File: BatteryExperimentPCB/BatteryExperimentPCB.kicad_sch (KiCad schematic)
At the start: 32 parts, among them J1 USB_C_Receptacle_USB2.0_14P, J2 Conn_01x12_Pin, J3 Conn_01x12_Pin, Q1 DMG1012T, SW1 SW_Push, U1 ATtiny3226-M, U2 USBLC6-2P6, U3 BQ25628RYKR

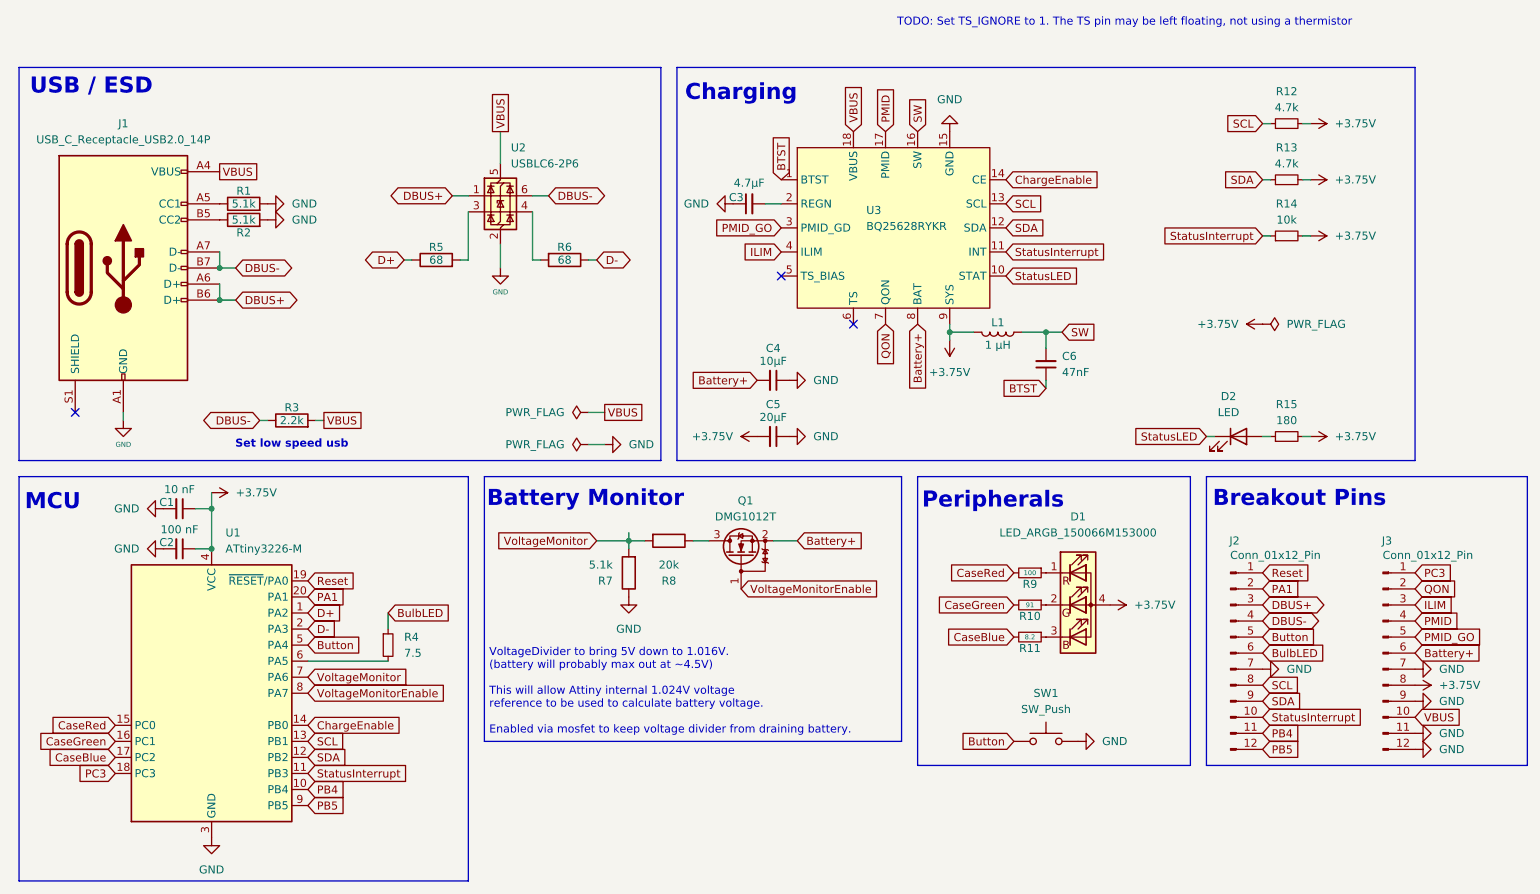
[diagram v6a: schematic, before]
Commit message: updating comment, changing pin breakout order
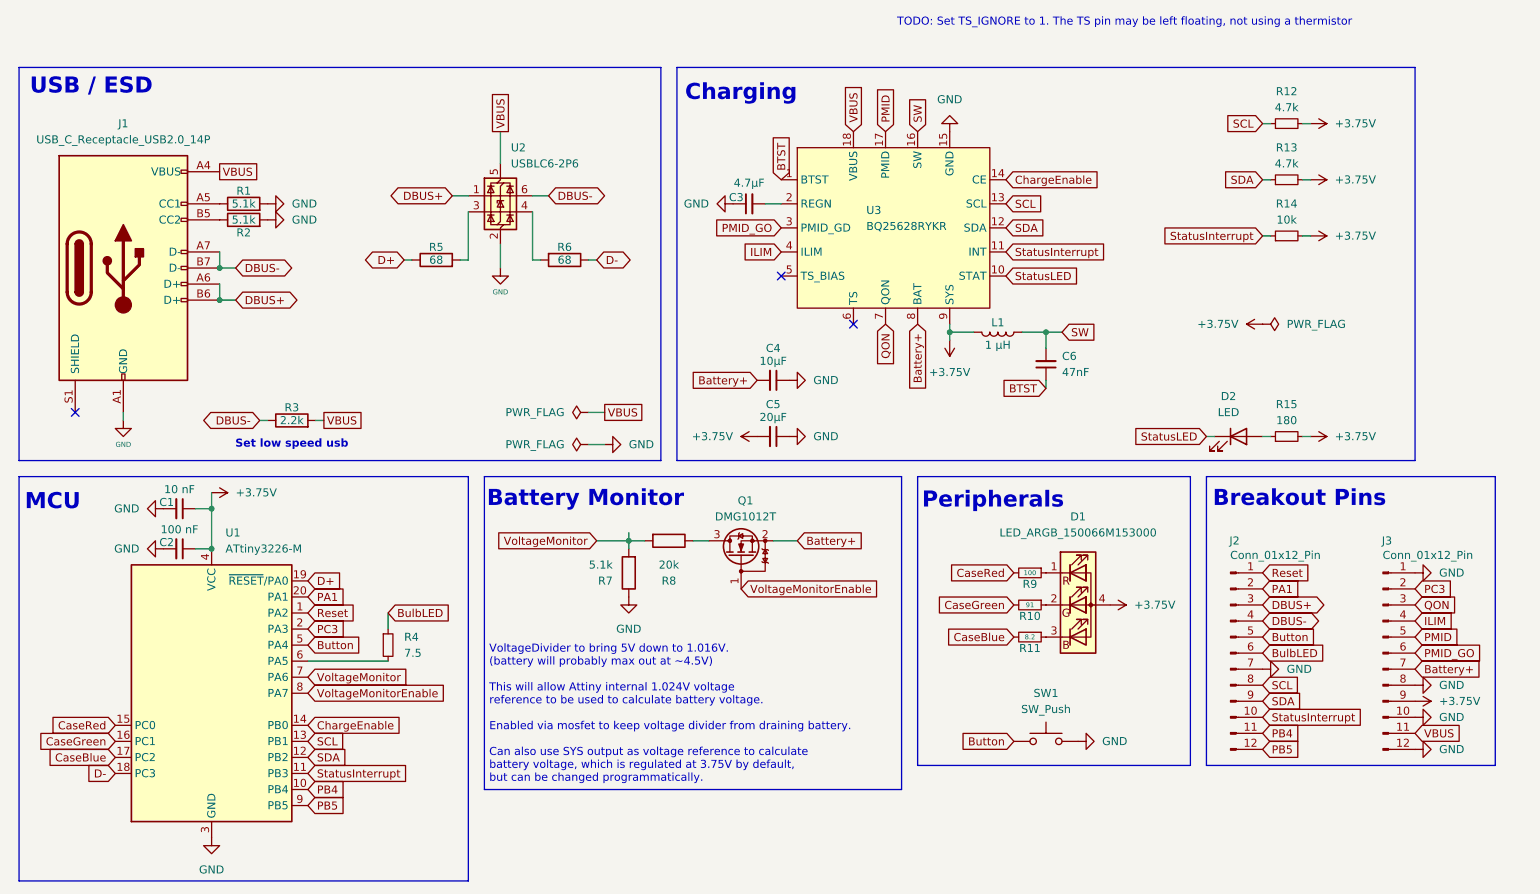
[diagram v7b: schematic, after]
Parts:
- C1, C2, C3, C4, C5, C6: footprint Capacitor_SMD:C_0805_2012Metric -> Capacitor_SMD:C_0603_1608Metric
- R1, R10, R11, R12, R13, R14, R15, R2, R3, R4, R5, R6, R7, R8, R9, SW1: footprint Resistor_SMD:R_0805_2012Metric -> Resistor_SMD:R_0603_1608Metric
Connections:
- net +3.75V: now also J3.9 (Pin_9); no longer J3.8 (Pin_8)
- net Battery+: now also J3.7 (Pin_7); no longer J3.6 (Pin_6)
- net D+: now also U1.19 (~{RESET}/PA0); no longer U1.1 (PA2)
- net D-: now also U1.18 (PC3); no longer U1.2 (PA3)
- net GND: now also J3.1 (Pin_1), J3.10 (Pin_10), J3.8 (Pin_8); no longer J3.11 (Pin_11), J3.7 (Pin_7), J3.9 (Pin_9)
- net ILIM: now also J3.4 (Pin_4); no longer J3.3 (Pin_3)
- net PC3: now also J3.2 (Pin_2), U1.2 (PA3); no longer J3.1 (Pin_1), U1.18 (PC3)
- net PMID: now also J3.5 (Pin_5); no longer J3.4 (Pin_4)
- net PMID_GO: now also J3.6 (Pin_6); no longer J3.5 (Pin_5)
- net QON: now also J3.3 (Pin_3); no longer J3.2 (Pin_2)
- net Reset: now also U1.1 (PA2); no longer U1.19 (~{RESET}/PA0)
- net VBUS: now also J3.11 (Pin_11); no longer J3.10 (Pin_10)
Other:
- note added: "VoltageDivider to bring 5V down to 1.016V. (battery will probably max out at ~4.5V) This will allow Attiny internal 1.024V voltage reference to be used to calculate battery voltage. Enabled via mosfet to keep voltage divider from draining battery. Can also use SYS output as voltage reference to calculate battery voltage, which is regulated at 3.75V by default, but can be changed programmatically."
- note removed: "VoltageDivider to bring 5V down to 1.016V. (battery will probably max out at ~4.5V) This will allow Attiny internal 1.024V voltage reference to be used to calculate battery voltage. Enabled via mosfet to keep voltage divider from draining battery."

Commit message: more pcb work
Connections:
- net Button: now also J2.2 (Pin_2), U1.2 (PA3); no longer J2.5 (Pin_5), U1.5 (PA4)
- net PA1: now also J2.5 (Pin_5); no longer J2.2 (Pin_2)
- net PC3 renamed PA4
- net PA4: now also U1.5 (PA4); no longer U1.2 (PA3)
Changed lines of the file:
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@@
-		)
-	)
-	(global_label "Button"
-		(shape input)
-		(at 59.69 105.41 0)
-		(fields_autoplaced yes)
-		(effects
-			(font
-				(size 1.27 1.27)
-			)
-			(justify left)
-		)
-		(property "Intersheetrefs" "${INTERSHEET_REFS}"
-			(at 68.8436 105.41 0)
-			(effects
-				(font
-					(size 1.27 1.27)
-				)
-				(justify left)
-				(hide yes)
-			)
 		)
 	)
@@
 		)
 	)
-	(global_label "PC3"
+	(global_label "PA4"
 		(shape input)
 		(at 234.95 96.52 0)
@@
 		)
 		(property "Intersheetrefs" "${INTERSHEET_REFS}"
-			(at 241.6847 96.52 0)
+			(at 241.5033 96.52 0)
 			(effects
 				(font
@@
 		)
 	)
+	(global_label "PA4"
+		(shape input)
+		(at 59.69 105.41 0)
+		(fields_autoplaced yes)
+		(effects
+			(font
+				(size 1.27 1.27)
+			)
+			(justify left)
+		)
+		(property "Intersheetrefs" "${INTERSHEET_REFS}"
+			(at 66.2433 105.41 0)
+			(effects
+				(font
+					(size 1.27 1.27)
+				)
+				(justify left)
+				(hide yes)
+			)
+		)
+	)
+	(global_label "SDA"
+		(shape input)
+		(at 210.82 31.75 180)
+		(fields_autoplaced yes)
+		(effects
+			(font
+				(size 1.27 1.27)
+			)
+			(justify right)
+		)
+		(property "Intersheetrefs" "${INTERSHEET_REFS}"
+			(at 204.2667 31.75 0)
+			(effects
+				(font
+					(size 1.27 1.27)
+				)
+				(justify right)
+				(hide yes)
+			)
+		)
+	)
 	(global_label "PA1"
 		(shape input)
-		(at 210.82 96.52 0)
-		(fields_autoplaced yes)
-		(effects
-			(font
-				(size 1.27 1.27)
-			)
-			(justify left)
-		)
-		(property "Intersheetrefs" "${INTERSHEET_REFS}"
-			(at 217.3733 96.52 0)
-			(effects
-				(font
-					(size 1.27 1.27)
-				)
-				(justify left)
-				(hide yes)
-			)
-		)
-	)
-	(global_label "SDA"
-		(shape input)
-		(at 210.82 31.75 180)
-		(fields_autoplaced yes)
-		(effects
-			(font
-				(size 1.27 1.27)
-			)
-			(justify right)
-		)
-		(property "Intersheetrefs" "${INTERSHEET_REFS}"
-			(at 204.2667 31.75 0)
-			(effects
-				(font
-					(size 1.27 1.27)
-				)
-				(justify right)
+		(at 210.82 104.14 0)
+		(fields_autoplaced yes)
+		(effects
+			(font
+				(size 1.27 1.27)
+			)
+			(justify left)
+		)
+		(property "Intersheetrefs" "${INTERSHEET_REFS}"
+			(at 217.3733 104.14 0)
+			(effects
+				(font
+					(size 1.27 1.27)
+				)
+				(justify left)
 				(hide yes)
 			)
@@
 		)
 	)
+	(global_label "Button"
+		(shape input)
+		(at 210.82 96.52 0)
+		(fields_autoplaced yes)
+		(effects
+			(font
+				(size 1.27 1.27)
+			)
+			(justify left)
+		)
+		(property "Intersheetrefs" "${INTERSHEET_REFS}"
+			(at 219.9736 96.52 0)
+			(effects
+				(font
+					(size 1.27 1.27)
+				)
+				(justify left)
+				(hide yes)
+			)
+		)
+	)
 	(global_label "CaseBlue"
 		(shape input)
@@
 		)
 	)
-	(global_label "Button"
-		(shape input)
-		(at 210.82 104.14 0)
-		(fields_autoplaced yes)
-		(effects
-			(font
-				(size 1.27 1.27)
-			)
-			(justify left)
-		)
-		(property "Intersheetrefs" "${INTERSHEET_REFS}"
-			(at 219.9736 104.14 0)
-			(effects
-				(font
-					(size 1.27 1.27)
-				)
-				(justify left)
-				(hide yes)
-			)
-		)
-	)
-	(global_label "PC3"
-		(shape input)
-		(at 59.69 102.87 0)
-		(fields_autoplaced yes)
-		(effects
-			(font
-				(size 1.27 1.27)
-			)
-			(justify left)
-		)
-		(property "Intersheetrefs" "${INTERSHEET_REFS}"
-			(at 66.4247 102.87 0)
-			(effects
-				(font
-					(size 1.27 1.27)
-				)
-				(justify left)
-				(hide yes)
-			)
-		)
-	)
 	(global_label "Battery+"
 		(shape input)
@@
 			(effects
 				(font
+					(size 1.27 1.27)
+				)
+				(justify left)
+				(hide yes)
+			)
+		)
+	)
+	(global_label "Button"
+		(shape input)
+		(at 59.69 102.87 0)
+		(fields_autoplaced yes)
+		(effects
+			(font
+				(size 1.27 1.27)
+			)
+			(justify left)
+		)
+		(property "Intersheetrefs" "${INTERSHEET_REFS}"
+			(at 68.8436 102.87 0)
+			(effects
+				(font
